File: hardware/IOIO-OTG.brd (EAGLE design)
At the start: 68.6 x 30.5 mm, 60 parts, among them Q1 IRLML2244, Q2 2N7002PW, Q3 AO3404A, U1 PIC24FJ256GB206, U2 TPS62133RGTT, U3 VREG_MIC5216

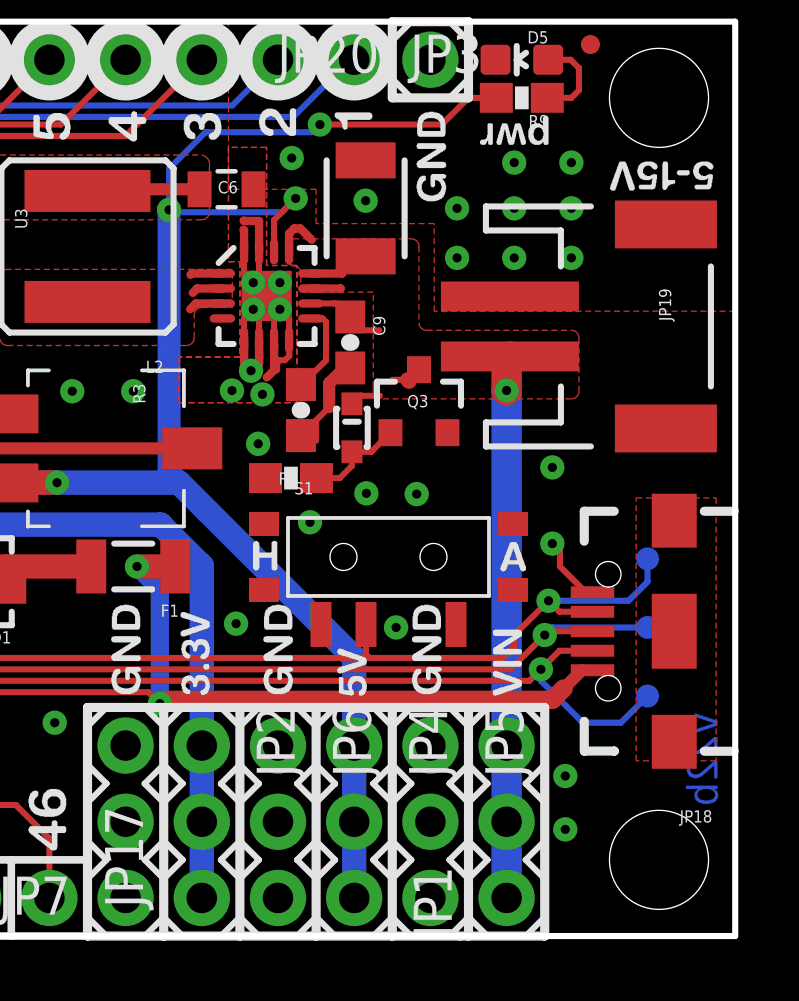
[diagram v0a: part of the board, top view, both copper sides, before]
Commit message: swapping out devices to include PROD_IDs
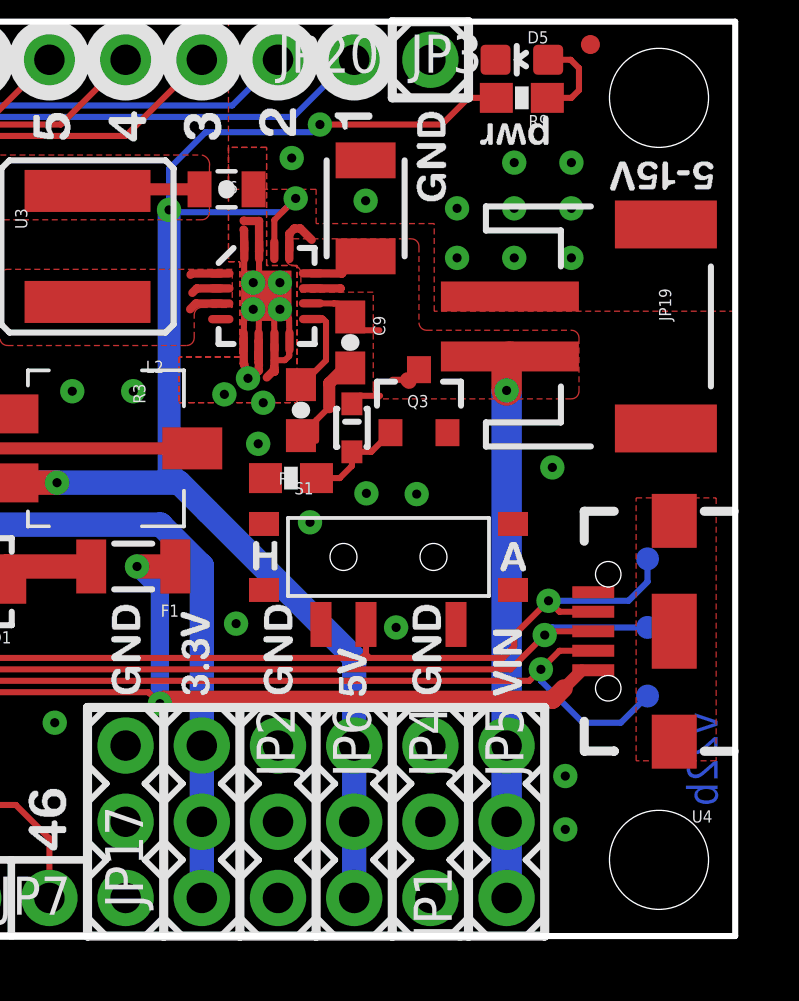
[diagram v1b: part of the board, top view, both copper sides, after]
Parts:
- removed JP18: (no value), SparkFun-Connectors:USB-B-MICRO-SMD_V03
- added U4: (no value), SparkFun-Connectors:USB-AB-MICRO-SMD_V03
- C10: device SparkFun-Passives:EIA3216 -> SparkFun-Capacitors:EIA3216
- C6: device SparkFun-Passives:0805 -> SparkFun-Capacitors:0805-CAP
- C7: device SparkFun:EIA3216 -> SparkFun-Capacitors:EIA3216
- JP19: value JST Connector -> JST; device SparkFun:JST-2-SMD -> SparkFun-Connectors:JST-2-SMD
- U2: device SparkFun-PowerIC:QFN16-3X3MM -> SparkFun-PowerIC:QFN16-3X3MM_1:1_V03
- U3: value VREG_MIC5216 -> V_REG_MIC5216
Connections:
- net ANCHOR1: now also U4.SHIELD1, U4.SHIELD2, U4.SHIELD3; no longer JP18.SHIELD1, JP18.SHIELD2, JP18.SHIELD3
- net D+: now also U4.D+1; no longer JP18.D+1
- net D-: now also U4.D-1; no longer JP18.D-1
- net GND: now also U4.GND1; no longer JP18.GND1
- net USBID: now also U4.ID1; no longer JP18.ID1
- net VBUS: now also U4.VBUS1; no longer JP18.VBUS1
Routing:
- net GND: track 53.7 -> 52.2 mm, vias 81 -> 80

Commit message: more PROD_IDs
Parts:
- C11: device SparkFun-Passives:1210 -> SparkFun-Capacitors:1210
- S1: value (none) -> SWITCH_SPDT
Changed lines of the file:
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@@
 <setting verticaltext="up"/>
 </settings>
-<grid distance="0.05" unitdist="inch" unit="inch" style="lines" multiple="2" display="yes" altdistance="0.0001" altunitdist="inch" altunit="inch"/>
+<grid distance="0.05" unitdist="inch" unit="inch" style="lines" multiple="2" display="yes" altdistance="0.005" altunitdist="inch" altunit="inch"/>
 <layers>
 <layer number="1" name="Top" color="4" fill="1" visible="yes" active="yes"/>
-<layer number="16" name="Bottom" color="1" fill="1" visible="no" active="yes"/>
+<layer number="16" name="Bottom" color="1" fill="1" visible="yes" active="yes"/>
 <layer number="17" name="Pads" color="2" fill="1" visible="yes" active="yes"/>
 <layer number="18" name="Vias" color="2" fill="1" visible="yes" active="yes"/>
@@
 <layer number="20" name="Dimension" color="15" fill="1" visible="yes" active="yes"/>
 <layer number="21" name="tPlace" color="16" fill="1" visible="yes" active="yes"/>
-<layer number="22" name="bPlace" color="14" fill="1" visible="no" active="yes"/>
+<layer number="22" name="bPlace" color="14" fill="1" visible="yes" active="yes"/>
 <layer number="23" name="tOrigins" color="15" fill="1" visible="yes" active="yes"/>
 <layer number="24" name="bOrigins" color="15" fill="1" visible="yes" active="yes"/>
@@
 <layer number="47" name="Measures" color="7" fill="1" visible="no" active="yes"/>
 <layer number="48" name="Document" color="7" fill="1" visible="no" active="yes"/>
-<layer number="49" name="Reference" color="7" fill="1" visible="yes" active="yes"/>
+<layer number="49" name="Reference" color="7" fill="1" visible="no" active="yes"/>
 <layer number="50" name="dxf" color="7" fill="1" visible="no" active="yes"/>
-<layer number="51" name="tDocu" color="6" fill="1" visible="no" active="yes"/>
+<layer number="51" name="tDocu" color="6" fill="1" visible="yes" active="yes"/>
 <layer number="52" name="bDocu" color="7" fill="1" visible="no" active="yes"/>
 <layer number="57" name="tCAD" color="7" fill="1" visible="no" active="no"/>
@@
 <attribute name="NAME" x="23.114" y="19.482640625" size="0.4064" layer="25" rot="R315"/>
 <attribute name="VALUE" x="18.87135625" y="15.24" size="0.4064" layer="27" rot="R315"/>
-<attribute name="PROD_ID" value="IC-10386" x="23.114" y="15.24" size="1.778" layer="27" rot="R315" display="off"/>
+<attribute name="PROD_ID" value="IC-11312" x="23.114" y="15.24" size="1.778" layer="27" rot="R315" display="off"/>
 </element>
 <element name="C1" library="SparkFun-Capacitors" package="0603-CAP" value="0.1uF" x="26.768515625" y="6.630671875" smashed="yes" rot="R315">
@@
 <element name="Q1" library="SparkFun-DiscreteSemi" package="SOT23-3" value="IRLML2244" x="40.64" y="15.113" smashed="yes" rot="R270">
 <attribute name="NAME" x="42.418" y="15.9385" size="0.4064" layer="25" rot="R270"/>
+<attribute name="PROD_ID" value="TRANS-11153" x="40.64" y="15.113" size="1.778" layer="27" rot="R270" display="off"/>
 </element>
 <element name="Q2" library="SparkFun-DiscreteSemi" package="SOT323" value="2N7002PW" x="40.513" y="18.161" smashed="yes" rot="R270">
@@
 <attribute name="VALUE" x="41.8225" y="19.277" size="0.4064" layer="27" rot="R270"/>
 <attribute name="PART#" value="2N7002PW" x="39.37" y="16.51" size="1.778" layer="21" rot="R270" display="off"/>
+<attribute name="PROD_ID" value="TRANS-11151" x="40.513" y="18.161" size="1.778" layer="27" rot="R270" display="off"/>
 </element>
 <element name="D1" library="SparkFun-DiscreteSemi" package="SMA-DIODE" value="B340A" x="42.164" y="11.811" smashed="yes" rot="R180">
@@
 <attribute name="NAME" x="50.038" y="11.049" size="0.4064" layer="25" rot="R180"/>
 <attribute name="PART#" value="0ZCA0075FF2G" x="44.45" y="8.89" size="1.778" layer="21" rot="R180" display="off"/>
+<attribute name="PROD_ID" value="RES-11150" x="48.514" y="12.319" size="1.778" layer="27" rot="R180" display="off"/>
 </element>
 <element name="R2" library="SparkFun-Resistors" package="0603-RES" value="100k" x="29.4132" y="21.3614" smashed="yes" rot="R45">
@@
 <attribute name="PROD_ID" value="CAP-09633" x="54.104540625" y="17.531078125" size="1.778" layer="27" rot="R270" display="off"/>
 </element>
-<element name="C11" library="SparkFun-Passives" package="1210" value="10uF" x="56.261" y="24.257" smashed="yes" rot="R90">
-<attribute name="VALUE" x="56.961" y="23.357" size="0.4064" layer="27" rot="R90"/>
+<element name="C11" library="SparkFun-Capacitors" package="1210" value="10uF" x="56.261" y="24.257" smashed="yes" rot="R90">
+<attribute name="VALUE" value="10uF" x="56.961" y="23.357" size="0.4064" layer="27" rot="R90"/>
 <attribute name="PART#" value="UMK325C7106MM-T" x="46.482" y="15.367" size="1.778" layer="21" rot="R90" display="off"/>
+<attribute name="PROD_ID" value="CAP-09824" x="56.261" y="24.257" size="1.778" layer="27" rot="R90" display="off"/>
 </element>
 <element name="L2" library="SparkFun-Passives" package="CR54" value="VLC5045T-3R3N" x="46.99" y="22.987" smashed="yes" rot="R180">
 <attribute name="AM" value="3.3uH" x="46.99" y="22.987" size="1.778" layer="27" rot="R180" display="off"/>
 <attribute name="NAME" x="49.53" y="19.177" size="0.4064" layer="25" rot="R180"/>
+<attribute name="PROD_ID" value="NDUC-11157" x="46.99" y="22.987" size="1.778" layer="27" rot="R180" display="off"/>
 </element>
 <element name="U3" library="SparkFun-PowerIC" package="MSOP8" value="V_REG_MIC5216" x="42.037" y="22.987" smashed="yes" rot="R180">
@@
 <attribute name="PROD_ID" value="RES-07859" x="27.872515625" y="7.768040625" size="1.778" layer="27" rot="R315" display="off"/>
 </element>
-<element name="S1" library="SparkFun-Electromechanical" package="KPS-1290" value="" x="57.023" y="12.6365" smashed="yes" rot="R180">
+<element name="S1" library="SparkFun-Electromechanical" package="KPS-1290" value="SWITCH_SPDT" x="57.023" y="12.6365" smashed="yes" rot="R180">
 <attribute name="NAME" x="54.523" y="15.1285" size="0.4064" layer="25" rot="R180"/>
 <attribute name="VALUE" x="54.523" y="15.8665" size="0.4064" layer="27" rot="R180"/>
+<attribute name="PROD_ID" value="SWCH-10651" x="57.023" y="12.6365" size="1.778" layer="27" rot="R180" display="off"/>
 </element>
 <element name="JP9" library="SparkFun-Connectors" package="1X11_NO_SILK" value="" x="7.62" y="3.81" smashed="yes" rot="R90">

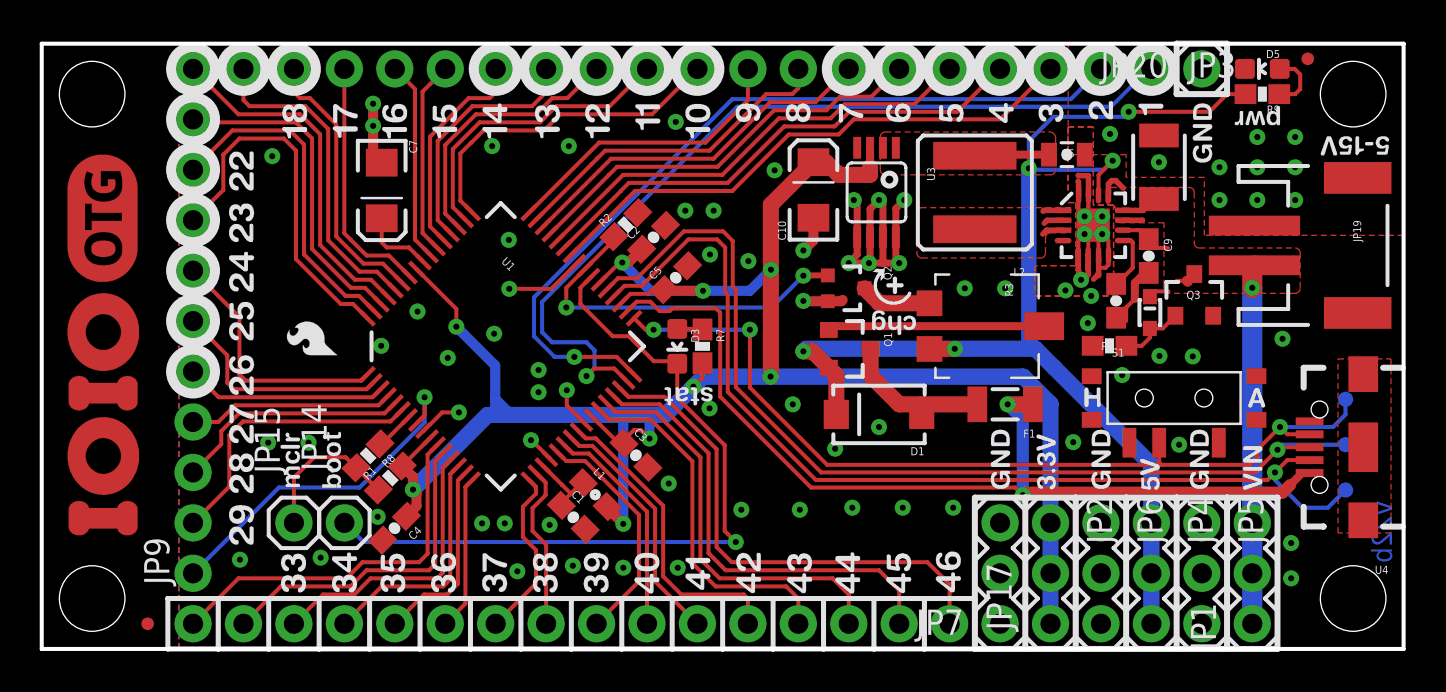
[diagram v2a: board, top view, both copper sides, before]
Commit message: Package update on D2 (zener) and PROD_IDs
Had to scoot upwards on most of the power circuit components to make
space for the correct package size on the zener.

All PROD_IDs done.
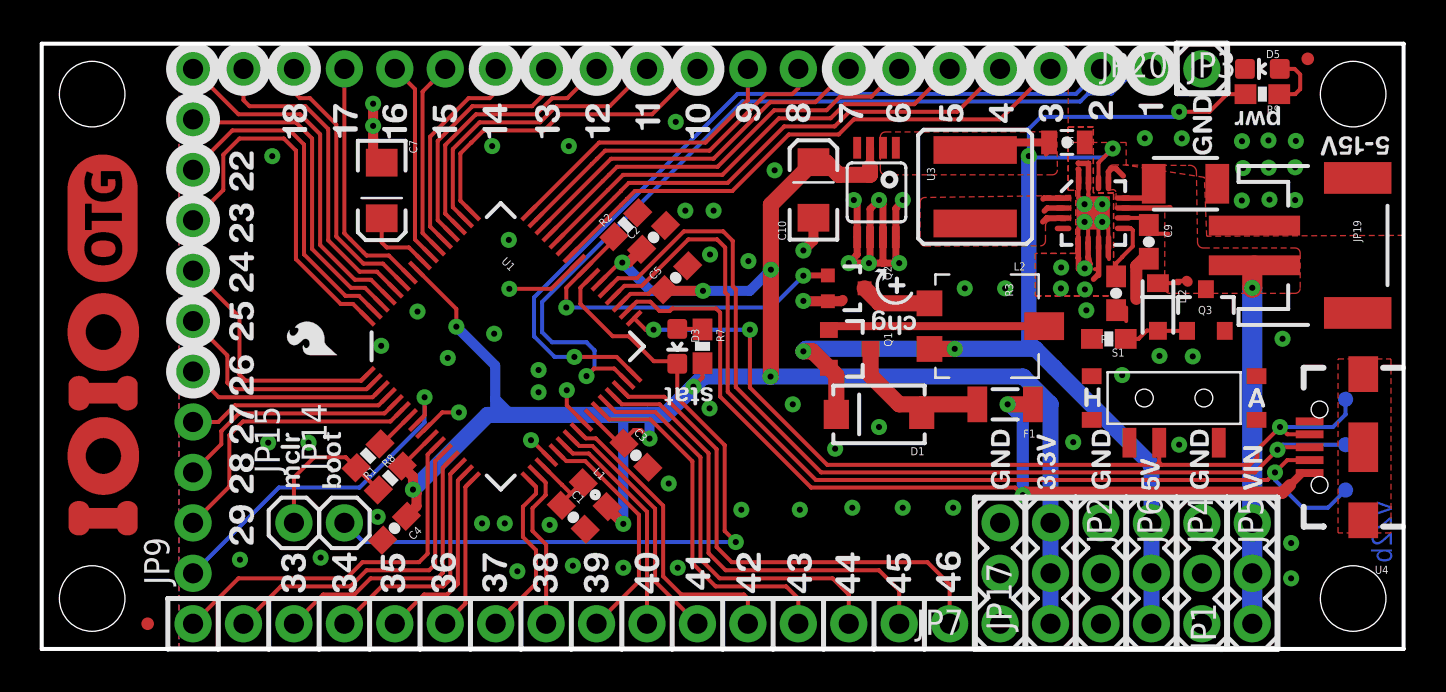
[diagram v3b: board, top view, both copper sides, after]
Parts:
- D2: device IOIO-OTG:SPARKFUN-DISCRETESEMI_SOD-523 -> SparkFun-DiscreteSemi:PANASONIC_SMINI2-F5-B
- Q3: value AO3404A -> MOSFET-NCHANNELAO3404A; device IOIO-OTG:SPARKFUN-DISCRETESEMI_SOT23-3 -> SparkFun-DiscreteSemi:SOT23-3
- moved C11 1.57 mm to (57.6, 23.4), turned to 0 degrees
- moved Q3 0.96 mm to (58.6, 17.0)
- moved C9 0.71 mm to (55.8, 20.5)
- moved C6 0.61 mm to (51.6, 25.5)
- moved U2 0.61 mm to (53.0, 22.0)
- moved D2 0.49 mm to (56.2, 17.2), turned to 270 degrees
- moved C8 0.38 mm to (54.1, 17.9)
- moved R4 0.35 mm to (53.7, 15.6)
- moved L2 0.29 mm to (47.0, 23.3)
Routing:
- net 5V: track 71.0 -> 67.9 mm
- net VIN: track 27.1 -> 28.5 mm
- net GND: track 52.2 -> 52.5 mm, vias 80 -> 82
